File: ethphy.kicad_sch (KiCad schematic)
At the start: 19 parts, among them J11 ARJM11A1-009-AB-EW2, U2 DP83848KSQ/NOPB

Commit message: Launchpad controller revision 06/03/2024
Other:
- note added: "Tie to VCC"

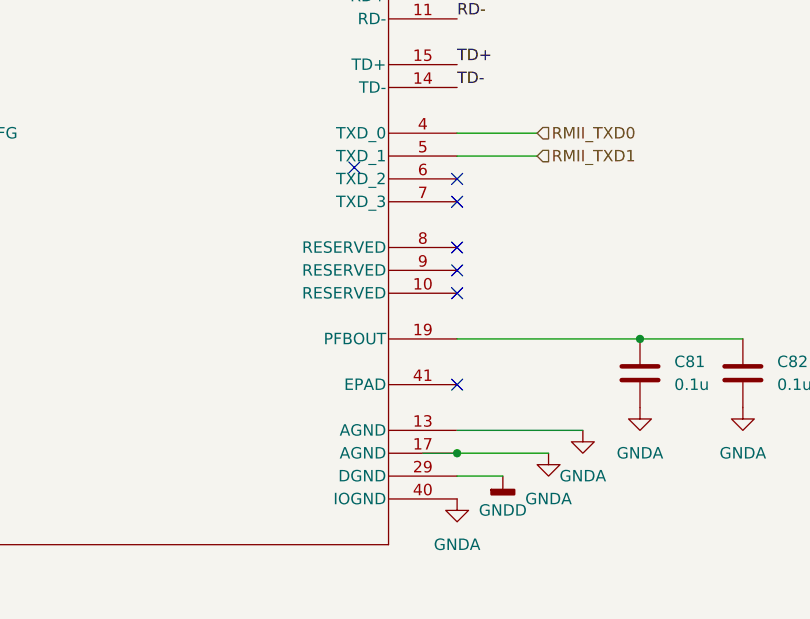
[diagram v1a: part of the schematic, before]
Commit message: added footprints to almost all components
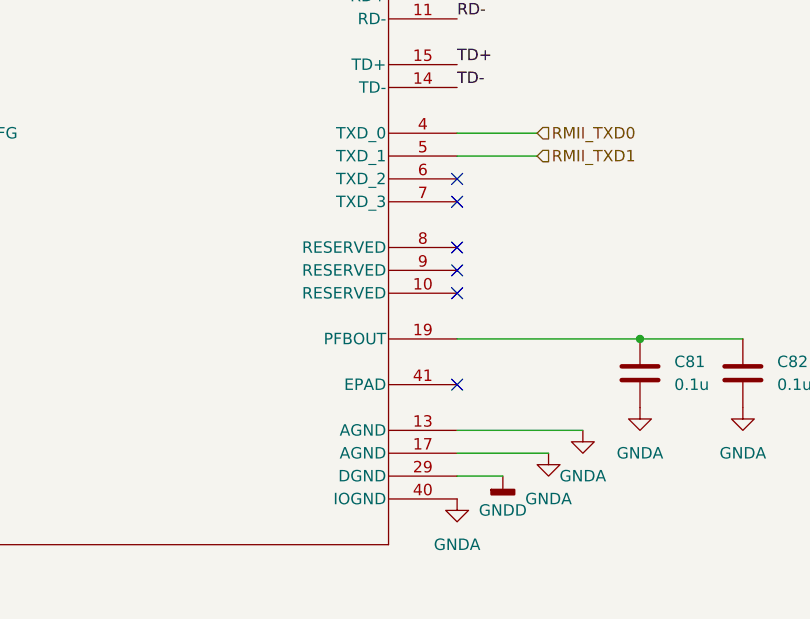
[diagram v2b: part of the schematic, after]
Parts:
- C79, C80, C81, C82, C87, C88, C89, C90: footprint (none) -> Capacitor_SMD:C_0603_1608Metric_Pad1.08x0.95mm_HandSolder
- R17, R18, R19, R20, R21, R58, R59, R60, R61: footprint (none) -> Resistor_SMD:R_0805_2012Metric_Pad1.20x1.40mm_HandSolder
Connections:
- no-connect marks 15 -> 14
